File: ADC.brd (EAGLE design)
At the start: 100 x 80 mm, 40 parts, among them IC1 AD8221ARZ, IC2 TLC2254ID, Q1 8MHz

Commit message: .
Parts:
- removed U$1: ADS1256IDBT, nanoeeg:SSOP28
- added C14: 4n7, rcl:C0805
- added C15, C16, C17, C18: 0.1, rcl:C0805
- added DC1: TMV0505D, dc-dc-converter:NMA
- added IC3: ADS1256IDBT, nanoeeg:ADS1256IDBT
- added IC4: AD8605ARTZ, nanoeeg:AD8605ARTZ
- added IC5: TS5A23157DGSR, nanoeeg:TS5A23157DGSR
- added IC6: ADUM1402ARWZ, nanoeeg:ADUM1402ARWZ
- added INT: (no value), pinhead:1X08
- added R18, R20: 10K, rcl:R0805
- added R19: 40K, rcl:R0805
- added R21: 124K, rcl:R0805
- added R22, R23, R25: 1K, rcl:R0805
- added R24: 3K, rcl:R0805
- IC2: device nanoeeg:SO-14DW -> nanoeeg:TLC2254ID
- moved C6 20.6 mm to (17.8, 32.4), turned to 90 degrees
- moved C11 17.7 mm to (17.1, 21.0)
- moved R13 14.7 mm to (10.2, 37.5), turned to 0 degrees
- moved C8 10.3 mm to (5.08, 49.5), turned to 270 degrees
- moved R11 4.49 mm to (11.4, 29.8)
- moved R10 4.02 mm to (14.6, 31.8), turned to 180 degrees
- moved C7 3.81 mm to (27.9, 40.6)
- moved R12 3.70 mm to (8.89, 28.6), turned to 90 degrees
- moved IC2 1.27 mm to (17.8, 26.0)
- moved C13 0.63 mm to (11.4, 25.4)
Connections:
- removed net N$18 (its old number): C12.2, C13.1, R12.2
- new net CH1SW1: IC2.7, IC5.9, R11.1, R12.2, R19.2
- new net CH1SW2: IC5.10, R19.1, R20.2
- new net CH2SW1: IC5.7
- new net CH2SW2: IC5.6
- new net N$15: C13.2, IC2.5, R13.1
- new net N$16: IC2.6, R10.2, R11.2
- new net N$17: C12.2, C13.1, R12.1
- new net N$28: C14.2, IC2.1, R21.1, R22.2
- new net N$29: C14.1, IC2.2, R20.1, R21.2
- new net N$30: IC4.4, R22.1, R25.1
- new net N$31: IC3.25, IC5.1, IC5.5
- new net N$32: IC6.3, R14.2
- new net N$33: IC6.4, R17.2
- new net N$34: IC6.5, R15.2
- new net N$35: IC6.6, R16.2
- new net N$36: DC1.1, INT.1
- new net N$37: C18.2, DC1.2, IC6.15, IC6.9, INT.3, INT.8
- new net N$38: C18.1, IC6.10, IC6.16, INT.2
- new net N$40: IC6.11, INT.7
- new net N$41: IC6.12, INT.6
- new net N$42: IC6.13, INT.5
- new net N$43: IC6.14, INT.4
- new net VREF: C16.1, IC3.4, R24.1
- net +3.3V: now also C17.1, IC3.14, IC3.15, IC3.16, IC5.8, IC6.1, IC6.7; no longer U$1.14, U$1.15, U$1.16
- net +5VA: now also C15.1, IC3.1, IC4.5; no longer U$1.1
- net GND: now also C15.2, C16.2, C17.2, DC1.5, IC3.17, IC3.2, IC3.20, IC3.3, IC4.2, IC5.3, IC6.2, IC6.8, R13.2, R18.1, R23.2; no longer R13.1, U$1.17, U$1.2
- net N$11: now also IC3.21; no longer U$1.21
- net N$12: now also IC3.18; no longer U$1.18
- net N$13: now also IC3.19; no longer U$1.19
- net N$14: now also IC3.24; no longer U$1.24
- net N$19: now also IC4.3, R23.1, R24.2; no longer IC2.1, R11.1, R12.1
- net N$20: now also R18.2; no longer C13.2, R13.2
- net N$21: now also IC3.6, IC4.1, R25.2; no longer IC2.2, R10.2, R11.2
- net N$22: now also IC3.23; no longer U$1.23
- net N$23: now also IC3.22; no longer U$1.22
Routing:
- net N$17: track 0.00 -> 15.9 mm
- net N$18: track 7.65 -> 0.00 mm
- net N$15: track 0.00 -> 6.81 mm
- net N$16: track 0.00 -> 6.39 mm
- net CH1SW1: track 0.00 -> 5.71 mm
- net GND: track 28.7 -> 31.4 mm
- net -5VA: track 22.7 -> 24.2 mm
- net N$26: track 20.8 -> 22.0 mm

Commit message: Circuit alpha version; routing in progress
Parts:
- removed DC1: TMV0505D, dc-dc-converter:NMA
- added C100, C114, C128, C41, C58, C72, C86: 47n, rcl:C0805
- added C101, C115, C129, C42, C56, C59, C73, C87: 33n, rcl:C0805
- added C102, C106, C107, C108, C109, C112, C113, C116, C120, C121, C122, C123, C126, C127, C130, C19, C24, C25, C26, C28, C33, C34, C35, C36, C39, C40, C43, C44, C48, C49, C50, C51, C52, C55, C57, C60, C64, C65, C66, C67, C70, C71, C74, C78, C79, C80, C81, C84, C85, C88, C92, C93, C94, C95, C98, C99: 0.1, rcl:C0805
- added C103, C117, C30, C45, C61, C75, C89: 10pF, rcl:C0805
- added C104, C105, C118, C119, C31, C32, C46, C47, C62, C63, C76, C77, C90, C91: 100pF, rcl:C0805
- added C110, C111, C124, C125, C37, C38, C53, C54, C68, C69, C82, C83, C96, C97: 1u, rcl:C0805
- added C20, C21, C22, C23, C27, C29: 47u, rcl:E2-4
- added D10, D11, D12, D13, D14, D15, D16, D17, D18, D19, D20, D21, D22, D23, D24, D25, D26, D27, D28, D29, D30, D31, D32, D5, D6, D7, D8, D9: BAV199, diode:SOT23
- added G1: TMV0505D, nanoeeg:TMV0505D
- added IC10, IC13, IC16, IC19, IC22, IC25, IC28: AD8605ARTZ, nanoeeg:AD8605ARTZ
- added IC11, IC14, IC17, IC20, IC23, IC26, IC8: AD8221ARZ, nanoeeg:SO-08
- added IC12, IC15, IC18, IC21, IC24, IC27, IC9: TLC2254ID, nanoeeg:TLC2254ID
- added IC7: REF3125AIDBZT, nanoeeg:REF3125AIDBZT
- added IN2: IN2, pinhead:1X04
- added IN3: IN3, pinhead:1X04
- added IN4: IN4, pinhead:1X04
- added IN5: IN5, pinhead:1X04
- added IN6: IN6, pinhead:1X04
- added IN7: IN7, pinhead:1X04
- added IN8: IN8, pinhead:1X04
- added L1, L2: 100uH, rcl:L4532P
- added R100, R119, R120, R139, R140, R159, R160, R39, R40, R59, R60, R79, R80, R99: 1K, rcl:R0805
- added R101, R102, R103, R112, R113, R114, R117, R118, R121, R122, R123, R132, R133, R134, R137, R138, R141, R142, R143, R152, R153, R154, R157, R158, R161, R162, R163, R32, R33, R34, R37, R38, R41, R42, R43, R52, R53, R54, R57, R58, R61, R62, R63, R72, R73, R74, R77, R78, R81, R82, R83, R92, R93, R94, R97, R98: 100K, rcl:R0805
- added R104, R107, R108, R124, R127, R128, R144, R147, R148, R164, R27, R28, R44, R47, R48, R64, R67, R68, R84, R87, R88: 100, rcl:R0805
- added R105, R106, R109, R110, R125, R126, R129, R130, R145, R146, R149, R150, R26, R29, R30, R45, R46, R49, R50, R65, R66, R69, R70, R85, R86, R89, R90: 2K2, rcl:R0805
- added R111, R131, R151, R31, R51, R71, R91: 2K, rcl:R0805
- added R115, R135, R155, R35, R55, R75, R95: 910K, rcl:R0805
- added R116, R136, R156, R36, R56, R76, R96: 680K, rcl:R0805
- C10, C9: value 10pF -> 18p
- C12, C13: value 1 -> 1u
- C14: value 4n7 -> 47n
- COM: value (none) -> COM
- IC5: value TS5A23157DGSR -> MCP170333MB; device nanoeeg:TS5A23157DGSR -> linear:SOT89
- IN1: value (none) -> IN1
- INT: value (none) -> INT
- R18: value 10K -> 100
- R19: value 40K -> 100K
- R20: value 10K -> 100K
- R21: value 124K -> 100K
- R23: value 1K -> 100K
- R24: value 3K -> 2K2
- moved INT 144.8 mm to (114.9, 74.3), turned to 180 degrees
- moved C18 96.6 mm to (38.7, 74.9)
- moved R18 77.3 mm to (-4.45, 37.5)
- moved IC6 71.3 mm to (118.7, 52.1), flipped to the bottom
- moved IC5 69.3 mm to (88.3, 66.7), turned to 0 degrees
- moved C14 46.5 mm to (-4.45, 50.2), turned to 0 degrees
- moved C17 45.3 mm to (3.17, 40.0)
- moved R23 41.0 mm to (-4.45, 56.5), turned to 0 degrees
- moved R21 40.9 mm to (-4.45, 62.9), turned to 0 degrees
- moved R19 39.5 mm to (-4.45, 69.2), turned to 0 degrees
- moved R24 35.5 mm to (28.6, 6.03), flipped to the bottom
- moved Q1 19.9 mm to (13.3, 68.6), turned to 0 degrees
- moved R15 14.8 mm to (27.3, 68.6)
- moved R16 14.7 mm to (30.5, 76.8)
- moved R14 9.16 mm to (16.5, 76.8)
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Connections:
- removed net CH2SW1: IC5.7
- removed net CH2SW2: IC5.6
- new net CH1SW3: IC12.7, R55.1, R56.2, R58.2
- new net CH1SW4: IC15.7, R75.1, R76.2, R78.2
- new net CH1SW5: IC18.7, R95.1, R96.2, R98.2
- new net CH1SW6: IC21.7, R115.1, R116.2, R118.2
- new net CH1SW7: IC24.7, R135.1, R136.2, R138.2
- new net CH1SW8: IC27.7, R155.1, R156.2, R158.2
- new net N$100: IC14.2, IC15.10, R71.2
- new net N$101: IC14.3, IC15.12, R71.1
- new net N$102: IC14.4, R70.2
- new net N$103: D16.3, IC15.13, IC15.14, R68.2, R73.1
- new net N$104: D15.3, IC15.8, IC15.9, R67.2, R72.1
- new net N$105: C69.2, IC15.5, R77.1
- new net N$106: IC15.6, R74.2, R75.2
- new net N$107: C68.2, C69.1, R76.1
- new net N$108: C68.1, IC14.7
- new net N$109: C72.1, IC15.3, R81.1
- new net N$110: IC16.4, R79.1, R80.1
- new net N$111: IC16.1, R80.2, R84.2
- new net N$112: IC15.2, R82.1, R83.1
- new net N$113: C73.1, R78.1, R81.2
- new net N$114: C73.2, IC15.1, R79.2, R83.2
- new net N$115: C74.2, IC3.9, R84.1
- new net N$116: IN5.2, R88.1
- new net N$117: IN5.4, R85.1
- new net N$118: IN5.1, R86.1
- new net N$119: IC17.1, R89.2
- new net N$120: C75.1, C76.1, D17.3, R85.2, R89.1
- new net N$121: C75.2, C77.2, D18.3, R86.2, R90.1
- new net N$122: IC17.2, IC18.10, R91.2
- new net N$123: IC17.3, IC18.12, R91.1
- new net N$124: IC17.4, R90.2
- new net N$125: D20.3, IC18.13, IC18.14, R88.2, R93.1
- new net N$126: D19.3, IC18.8, IC18.9, R87.2, R92.1
- new net N$127: C83.2, IC18.5, R97.1
- new net N$128: IC18.6, R94.2, R95.2
- new net N$129: C82.2, C83.1, R96.1
- new net N$130: C82.1, IC17.7
- new net N$131: C86.1, IC18.3, R101.1
- new net N$132: IC19.4, R100.1, R99.1
- new net N$133: IC19.1, R100.2, R104.2
- new net N$134: IC18.2, R102.1, R103.1
- new net N$135: C87.1, R101.2, R98.1
- new net N$136: C87.2, IC18.1, R103.2, R99.2
- new net N$137: C88.2, IC3.10, R104.1
- new net N$138: IN6.3, R107.1
- new net N$139: IN6.2, R108.1
- new net N$140: IN6.4, R105.1
- new net N$141: IN6.1, R106.1
- new net N$142: IC20.1, R109.2
- new net N$143: C89.1, C90.1, D21.3, R105.2, R109.1
- new net N$144: C89.2, C91.2, D22.3, R106.2, R110.1
- new net N$145: IC20.2, IC21.10, R111.2
- new net N$146: IC20.3, IC21.12, R111.1
- new net N$147: IC20.4, R110.2
- new net N$148: D24.3, IC21.13, IC21.14, R108.2, R113.1
- new net N$149: D23.3, IC21.8, IC21.9, R107.2, R112.1
- new net N$150: C97.2, IC21.5, R117.1
- new net N$151: IC21.6, R114.2, R115.2
- new net N$152: C96.2, C97.1, R116.1
- new net N$153: C96.1, IC20.7
- new net N$154: C100.1, IC21.3, R121.1
- new net N$155: IC22.4, R119.1, R120.1
- new net N$156: IC22.1, R120.2, R124.2
- new net N$157: IC21.2, R122.1, R123.1
- new net N$158: C101.1, R118.1, R121.2
- new net N$159: C101.2, IC21.1, R119.2, R123.2
- new net N$160: C102.2, IC3.11, R124.1
- new net N$161: IN7.3, R127.1
- new net N$162: IN7.2, R128.1
- new net N$163: IN7.4, R125.1
- new net N$164: IN7.1, R126.1
- new net N$165: IC23.1, R129.2
- new net N$166: C103.1, C104.1, D25.3, R125.2, R129.1
- new net N$167: C103.2, C105.2, D26.3, R126.2, R130.1
- new net N$168: IC23.2, IC24.10, R131.2
- new net N$169: IC23.3, IC24.12, R131.1
- new net N$170: IC23.4, R130.2
- new net N$171: D28.3, IC24.13, IC24.14, R128.2, R133.1
- new net N$172: D27.3, IC24.8, IC24.9, R127.2, R132.1
- new net N$173: C111.2, IC24.5, R137.1
- new net N$174: IC24.6, R134.2, R135.2
- new net N$175: C110.2, C111.1, R136.1
- new net N$176: C110.1, IC23.7
- new net N$177: C114.1, IC24.3, R141.1
- new net N$178: IC25.4, R139.1, R140.1
- new net N$179: IC25.1, R140.2, R144.2
- new net N$180: IC24.2, R142.1, R143.1
- new net N$181: C115.1, R138.1, R141.2
- new net N$182: C115.2, IC24.1, R139.2, R143.2
- new net N$184: C130.2, IC3.13, R164.1
- new net N$185: IN8.3, R147.1
- new net N$186: IN8.2, R148.1
- new net N$187: IN8.4, R145.1
- new net N$188: IN8.1, R146.1
- new net N$189: IC26.1, R149.2
- new net N$190: C117.1, C118.1, D29.3, R145.2, R149.1
- new net N$191: C117.2, C119.2, D30.3, R146.2, R150.1
- new net N$192: IC26.2, IC27.10, R151.2
- new net N$193: IC26.3, IC27.12, R151.1
- new net N$194: IC26.4, R150.2
- new net N$195: D32.3, IC27.13, IC27.14, R148.2, R153.1
- new net N$196: D31.3, IC27.8, IC27.9, R147.2, R152.1
- new net N$197: C125.2, IC27.5, R157.1
- new net N$198: IC27.6, R154.2, R155.2
- new net N$199: C124.2, C125.1, R156.1
- new net N$200: C124.1, IC26.7
- new net N$201: C128.1, IC27.3, R161.1
- new net N$202: IC28.4, R159.1, R160.1
- new net N$203: IC28.1, R160.2, R164.2
- new net N$204: IC27.2, R162.1, R163.1
- new net N$205: C129.1, R158.1, R161.2
- new net N$206: C129.2, IC27.1, R159.2, R163.2
- new net N$39: C22.+, C24.1, G1.7, IC5.2@1, L1.2
- new net N$44: C23.-, C25.2, G1.5, L2.2
- new net N$45: IN2.2, R28.1
- new net N$46: IN2.4, R24.1
- new net N$47: IN2.1, R26.1
- new net N$48: IC8.1, R29.2
- new net N$49: C30.1, C31.1, D5.3, R24.2, R29.1
- new net N$50: C30.2, C32.2, D6.3, R26.2, R30.1
- new net N$51: IC8.2, IC9.10, R31.2
- new net N$52: IC8.3, IC9.12, R31.1
- new net N$53: IC8.4, R30.2
- new net N$54: D8.3, IC9.13, IC9.14, R28.2, R33.1
- new net N$55: D7.3, IC9.8, IC9.9, R27.2, R32.1
- new net N$56: C38.2, IC9.5, R37.1
- new net N$57: IC9.6, R34.2, R35.2
- new net N$58: C37.2, C38.1, R36.1
- new net N$59: C37.1, IC8.7
- new net N$60: C41.1, IC9.3, R41.1
- new net N$61: IC10.4, R39.1, R40.1
- new net N$62: IC10.1, R40.2, R44.2
- new net N$63: C56.2, IC2.1, R22.2, R23.2
- new net N$64: IC9.2, R42.1, R43.1
- new net N$65: C42.1, R38.1, R41.2
- new net N$66: C42.2, IC9.1, R39.2, R43.2
- new net N$67: C43.2, IC3.7, R44.1
- new net N$68: IN3.3, R47.1
- new net N$69: IN3.2, R48.1
- new net N$70: IN3.4, R45.1
- new net N$71: IN3.1, R46.1
- new net N$72: IC11.1, R49.2
- new net N$73: C45.1, C46.1, D9.3, R45.2, R49.1
- new net N$74: C45.2, C47.2, D10.3, R46.2, R50.1
- new net N$75: IC11.2, IC12.10, R51.2
- new net N$76: IC11.3, IC12.12, R51.1
- new net N$77: IC11.4, R50.2
- new net N$78: D12.3, IC12.13, IC12.14, R48.2, R53.1
- new net N$79: D11.3, IC12.8, IC12.9, R47.2, R52.1
- new net N$80: C54.2, IC12.5, R57.1
- new net N$81: IC12.6, R54.2, R55.2
- new net N$82: C53.2, C54.1, R56.1
- new net N$83: C53.1, IC11.7
- new net N$84: C58.1, IC12.3, R61.1
- new net N$85: IC13.4, R59.1, R60.1
- new net N$86: IC13.1, R60.2, R64.2
- new net N$87: IC12.2, R62.1, R63.1
- new net N$88: C59.1, R58.1, R61.2
- new net N$89: C59.2, IC12.1, R59.2, R63.2
- new net N$90: C60.2, IC3.8, R64.1
- new net N$91: C116.2, IC3.12, R144.1
- new net N$92: IN5.3, R87.1
- new net N$93: IN4.3, R67.1
- new net N$94: IN4.2, R68.1
- new net N$95: IN4.4, R65.1
- new net N$96: IN4.1, R66.1
- new net N$97: IC14.1, R69.2
- new net N$98: C61.1, C62.1, D13.3, R65.2, R69.1
- new net N$99: C61.2, C63.2, D14.3, R66.2, R70.1
- net +3.3V: now also C21.+, C44.1, IC5.3; no longer IC5.8
- net +5VA: now also C107.2, C108.1, C112.1, C121.2, C122.1, C126.1, C26.1, C27.+, C34.2, C35.1, C39.1, C49.2, C50.1, C55.1, C65.2, C66.1, C70.1, C79.2, C80.1, C84.1, C93.2, C94.1, C98.1, D10.2, D11.2, D12.2, D13.2, D14.2, D15.2, D16.2, D17.2, D18.2, D19.2, D20.2, D21.2, D22.2, D23.2, D24.2, D25.2, D26.2, D27.2, D28.2, D29.2, D30.2, D31.2, D32.2, D5.2, D6.2, D7.2, D8.2, D9.2, IC10.5, IC11.8, IC12.4, IC13.5, IC14.8, IC15.4, IC16.5, IC17.8, IC18.4, IC19.5, IC20.8, IC21.4, IC22.5, IC23.8, IC24.4, IC25.5, IC26.8, IC27.4, IC28.5, IC7.1, IC8.8, IC9.4, L1.1
- net -5VA: now also C106.1, C109.2, C120.1, C123.2, C28.2, C29.-, C33.1, C36.2, C48.1, C51.2, C64.1, C67.2, C78.1, C81.2, C92.1, C95.2, D10.1, D11.1, D12.1, D13.1, D14.1, D15.1, D16.1, D17.1, D18.1, D19.1, D20.1, D21.1, D22.1, D23.1, D24.1, D25.1, D26.1, D27.1, D28.1, D29.1, D30.1, D31.1, D32.1, D5.1, D6.1, D7.1, D8.1, D9.1, IC11.5, IC12.11, IC14.5, IC15.11, IC17.5, IC18.11, IC20.5, IC21.11, IC23.5, IC24.11, IC26.5, IC27.11, IC8.5, IC9.11, L2.1
- net CH1SW1: now also R20.2; no longer IC5.9, R19.2
- net CH1SW2: now also IC9.7, R35.1, R36.2, R38.2; no longer IC5.10, R19.1, R20.2
- net GND: now also C100.2, C102.1, C104.2, C105.1, C106.2, C107.1, C108.2, C109.1, C112.2, C113.1, C114.2, C116.1, C118.2, C119.1, C120.2, C121.1, C122.2, C123.1, C126.2, C127.1, C128.2, C130.1, C14.2, C19.1, C20.-, C21.-, C22.-, C23.+, C24.2, C25.1, C26.2, C27.-, C28.1, C29.+, C31.2, C32.1, C33.2, C34.1, C35.2, C36.1, C39.2, C40.1, C41.2, C43.1, C44.2, C46.2, C47.1, C48.2, C49.1, C50.2, C51.1, C52.1, C55.2, C57.1, C58.2, C60.1, C62.2, C63.1, C64.2, C65.1, C66.2, C67.1, C70.2, C71.1, C72.2, C74.1, C76.2, C77.1, C78.2, C79.1, C80.2, C81.1, C84.2, C85.1, C86.2, C88.1, C90.2, C91.1, C92.2, C93.1, C94.2, C95.1, C98.2, C99.1, G1.6, IC10.2, IC11.6, IC13.2, IC14.6, IC16.2, IC17.6, IC19.2, IC20.6, IC22.2, IC23.6, IC25.2, IC26.6, IC28.2, IC5.1, IC7.3, IC8.6, R102.2, R112.2, R113.2, R114.1, R117.2, R122.2, R132.2, R133.2, R134.1, R137.2, R142.2, R152.2, R153.2, R154.1, R157.2, R162.2, R21.2, R32.2, R33.2, R34.1, R37.2, R42.2, R52.2, R53.2, R54.1, R57.2, R62.2, R72.2, R73.2, R74.1, R77.2, R82.2, R92.2, R93.2, R94.1, R97.2; no longer DC1.5, IC5.3, R18.1, R23.2
- net N$19: now also IC2.2, R21.1; no longer IC4.3, R24.2
- net N$20: now also C14.1, R19.1; no longer R18.2
- net N$21: now also R18.2; no longer IC3.6
- net N$28: now also C19.2, IC3.6, R18.1; no longer C14.2, IC2.1, R21.1, R22.2
- net N$29: now also C56.1, R19.2; no longer C14.1, IC2.2, R21.2
- net N$31: now also IN2.3, R27.1; no longer IC3.25, IC5.1, IC5.5
- net N$36: now also G1.1; no longer DC1.1
- net N$37: now also G1.2; no longer DC1.2
- net VREF: now also C113.2, C127.2, C20.+, C40.2, C52.2, C57.2, C71.2, C85.2, C99.2, IC10.3, IC13.3, IC16.3, IC19.3, IC22.3, IC25.3, IC28.3, IC3.5, IC4.3, IC7.2; no longer R24.1
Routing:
- net GND: track 31.4 -> 188.8 mm, vias 1 -> 8
- net -5VA: track 24.2 -> 114.4 mm, vias 1 -> 4
- net +5VA: track 18.0 -> 97.5 mm, vias 1 -> 4
- net N$104: track 0.00 -> 22.9 mm, vias 0 -> 1
- net N$79: track 0.00 -> 22.9 mm, vias 0 -> 1
- net N$55: track 0.00 -> 22.5 mm, vias 0 -> 1
- net N$78: track 0.00 -> 21.6 mm, vias 0 -> 1
- net N$103: track 0.00 -> 21.6 mm, vias 0 -> 1
- net N$54: track 0.00 -> 21.3 mm, vias 0 -> 1
- net N$148: track 0.00 -> 15.0 mm
- net N$196: track 0.00 -> 15.0 mm
- net N$195: track 0.00 -> 15.0 mm
- net N$171: track 0.00 -> 15.0 mm
- net N$149: track 0.00 -> 15.0 mm
- net N$172: track 0.00 -> 15.0 mm
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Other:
- board size 100 x 80 mm -> 134.9 x 80 mm

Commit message: Filters are routed
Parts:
- moved C88 228.2 mm to (47.0, 123.8)
- moved R104 218.3 mm to (38.7, 138.4)
- moved C102 214.8 mm to (97.8, 153.7)
- moved C112 214.8 mm to (119.4, 186.1)
- moved C113 214.8 mm to (125.1, 186.1)
- moved C116 214.8 mm to (142.2, 186.1)
- moved C55 214.8 mm to (-2.54, 172.7)
- moved C70 214.8 mm to (46.4, 165.1)
- moved C71 214.8 mm to (10.2, 158.8)
- moved C74 214.8 mm to (25.4, 158.8)
- moved C84 214.8 mm to (69.8, 116.8)
- moved C85 214.8 mm to (33.7, 110.5)
- moved C98 214.8 mm to (100.3, 147.3)
- moved C99 214.8 mm to (105.4, 147.3)
- moved IC16 214.8 mm to (32.4, 203.8)
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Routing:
- net GND: track 188.8 -> 465.4 mm, vias 8 -> 24
- net +5VA: track 97.5 -> 183.6 mm, vias 4 -> 16
- net -5VA: track 114.4 -> 191.5 mm, vias 4 -> 8
- net N$75: track 2.61 -> 32.9 mm
- net N$51: track 2.61 -> 32.9 mm
- net N$168: track 2.61 -> 32.9 mm
- net N$145: track 2.61 -> 32.9 mm
- net N$122: track 2.61 -> 32.9 mm
- net N$100: track 2.61 -> 32.9 mm
- net N$192: track 2.61 -> 32.9 mm
- net N$169: track 2.61 -> 27.5 mm, vias 0 -> 2
- net N$52: track 2.61 -> 27.5 mm, vias 0 -> 2
- net N$123: track 2.61 -> 27.5 mm, vias 0 -> 2
- net N$76: track 2.61 -> 27.5 mm, vias 0 -> 2
- net N$146: track 2.61 -> 27.5 mm, vias 0 -> 2
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
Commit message: .
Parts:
- moved R140 108.9 mm to (123.2, 90.2)
- moved R40 102.5 mm to (27.3, 46.4), turned to 180 degrees
- moved IC22 102.3 mm to (104.1, 90.2)
- moved IC16 100.1 mm to (54.0, 106.0)
- moved R144 96.0 mm to (123.8, 96.5)
- moved C112 89.1 mm to (103.5, 98.4)
- moved C113 87.5 mm to (115.6, 99.1)
- moved C55 84.8 mm to (48.3, 104.8)
- moved C116 84.7 mm to (120.7, 104.1)
- moved R120 78.7 mm to (114.9, 94.6)
- moved C43 78.0 mm to (26.0, 92.7)
- moved C71 71.2 mm to (50.8, 100.3)
- moved R124 70.1 mm to (109.9, 98.4)
- moved C70 68.7 mm to (65.4, 99.1)
- moved C74 67.4 mm to (57.8, 99.7)
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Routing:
- net GND: track 465.4 -> 489.0 mm
- net N$37: track 0.00 -> 10.4 mm
- net N$40: track 0.00 -> 7.25 mm
- net N$43: track 0.00 -> 6.72 mm
- net N$41: track 0.00 -> 6.72 mm
- net N$42: track 0.00 -> 6.19 mm
- net N$36: track 0.00 -> 4.44 mm
- net +5VA: track 183.6 -> 184.2 mm
- net N$21: track 5.00 -> 5.63 mm
- net N$30: track 11.9 -> 12.5 mm
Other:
- board size 134.9 x 80 mm -> 132.1 x 82.5 mm

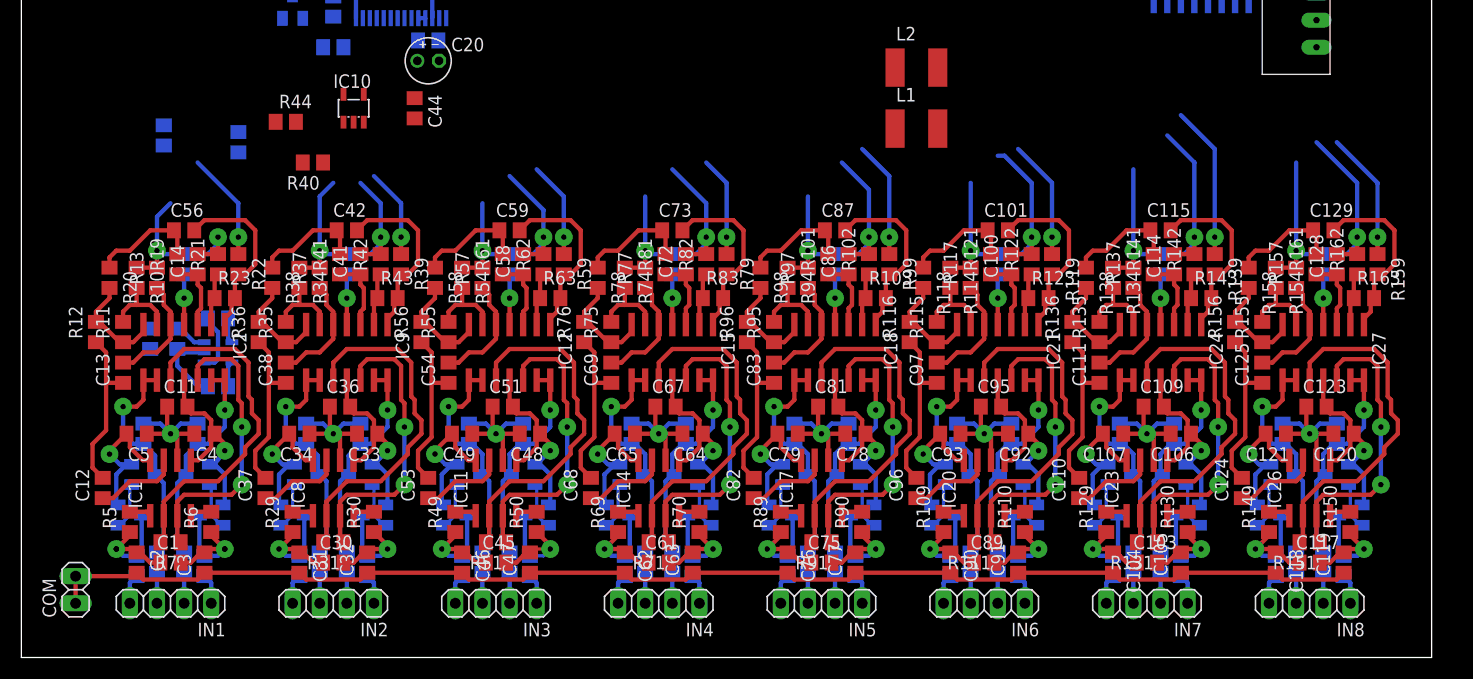
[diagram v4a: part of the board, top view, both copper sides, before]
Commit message: Some power lines routed
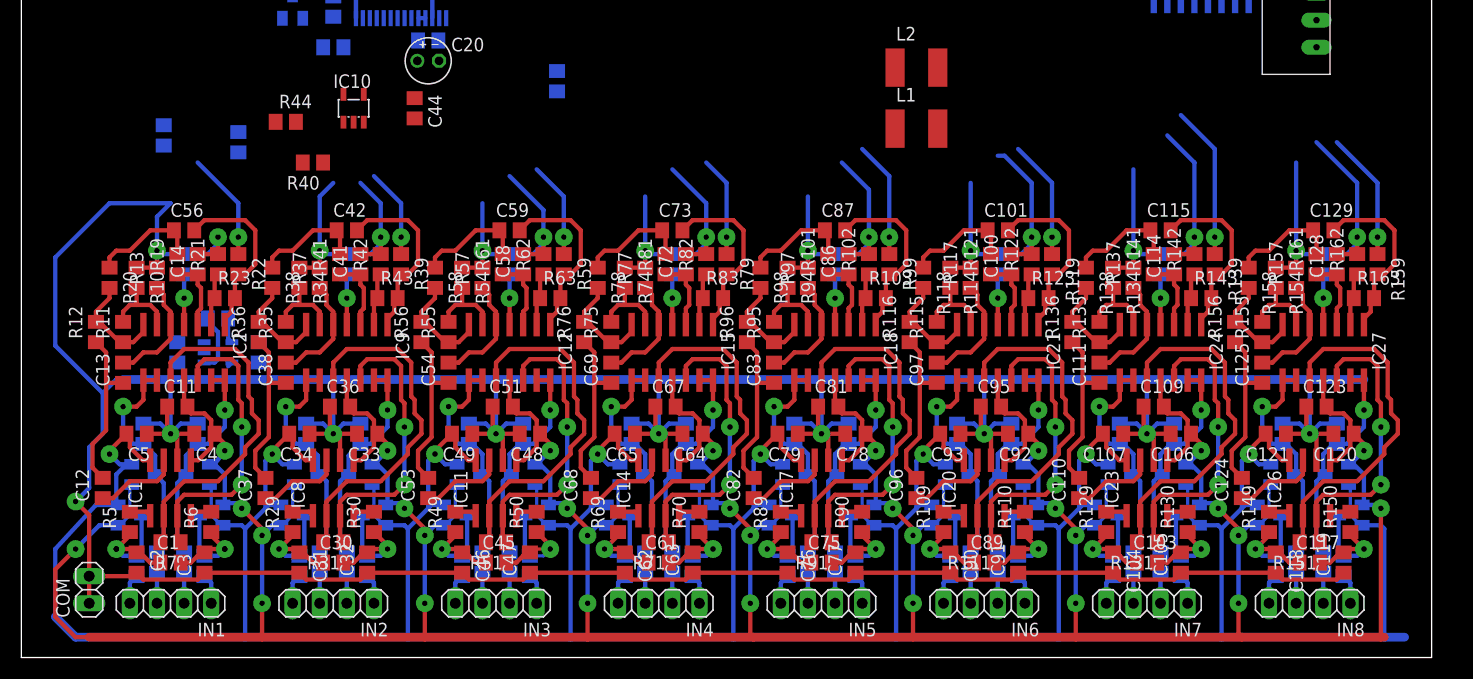
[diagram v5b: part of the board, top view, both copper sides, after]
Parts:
- moved C40 45.1 mm to (50.2, 54.0)
- moved C15 4.96 mm to (22.2, 28.6), turned to 270 degrees
- moved C52 1.27 mm to (14.6, 28.6)
- moved COM 1.27 mm to (6.35, 6.35)
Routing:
- net +5VA: track 184.2 -> 458.4 mm
- net -5VA: track 191.5 -> 460.6 mm, vias 8 -> 31
- net GND: track 489.0 -> 685.2 mm, vias 24 -> 25
- net VREF: track 3.69 -> 0.65 mm

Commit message: Latest modification for all-in-one board
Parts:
- moved INT 113.0 mm to (2.54, 50.2), turned to 270 degrees
- moved G1 106.2 mm to (15.2, 59.1), turned to 90 degrees
- moved IC6 97.9 mm to (14.0, 49.5), turned to 270 degrees
- moved C19 84.3 mm to (94.6, 71.1), flipped to the top
- moved R18 79.2 mm to (94.0, 77.5), flipped to the top
- moved C22 67.5 mm to (30.5, 55.2), turned to 90 degrees
- moved R40 65.7 mm to (79.4, 86.4)
- moved C21 63.6 mm to (36.8, 50.8), turned to 90 degrees
- moved C18 62.4 mm to (6.99, 41.9), flipped to the bottom, turned to 180 degrees
- moved IC7 58.6 mm to (83.8, 56.5)
- moved C24 57.4 mm to (27.9, 55.2), flipped to the bottom, turned to 90 degrees
- moved C40 56.2 mm to (96.5, 85.7), flipped to the top, turned to 270 degrees
- moved IC5 55.8 mm to (33.0, 50.8), flipped to the bottom, turned to 270 degrees
- moved R44 54.8 mm to (73.0, 76.2)
- moved IC10 52.9 mm to (74.3, 81.9)
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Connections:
- new net N$207: G1.2, INT.2
- net N$37: no longer G1.2, INT.3
- net N$38: now also INT.3; no longer INT.2
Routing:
- net +5VA: track 458.4 -> 616.0 mm, vias 16 -> 17
- net -5VA: track 460.6 -> 599.9 mm, vias 31 -> 33
- net GND: track 685.2 -> 730.5 mm, vias 25 -> 26
- net +3.3V: track 7.90 -> 36.2 mm
- net N$38: track 0.00 -> 26.5 mm, vias 0 -> 1
- net N$44: track 0.00 -> 22.4 mm, vias 0 -> 1
- net N$39: track 0.00 -> 20.2 mm, vias 0 -> 1
- net N$37: track 10.4 -> 22.0 mm
- net N$178: track 14.3 -> 4.13 mm
- net N$207: track 0.00 -> 9.42 mm
- net VREF: track 0.65 -> 9.49 mm
- net N$202: track 12.1 -> 4.13 mm
- net N$13: track 0.00 -> 7.78 mm
- net N$12: track 0.00 -> 7.75 mm
- net N$155: track 11.2 -> 4.13 mm
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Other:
- board size 132.1 x 82.5 mm -> 132.1 x 64.1 mm
